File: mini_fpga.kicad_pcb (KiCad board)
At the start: 4 copper layers, 50.8 x 50.8 mm, 130 parts, among them J1 PWR_HEADER1X6, J2 1X6_HEADER, J3 1X6_HEADER, J4 JTAG_1X6, J5 USD_SLOT, J6 HDMI, U1 AP7331, U2 PAM2306D, U3 XC6SLX9, U4 IS43R86400D-6TL, U5 S25FL164, U6 CPPC7, U7 FXMHD103

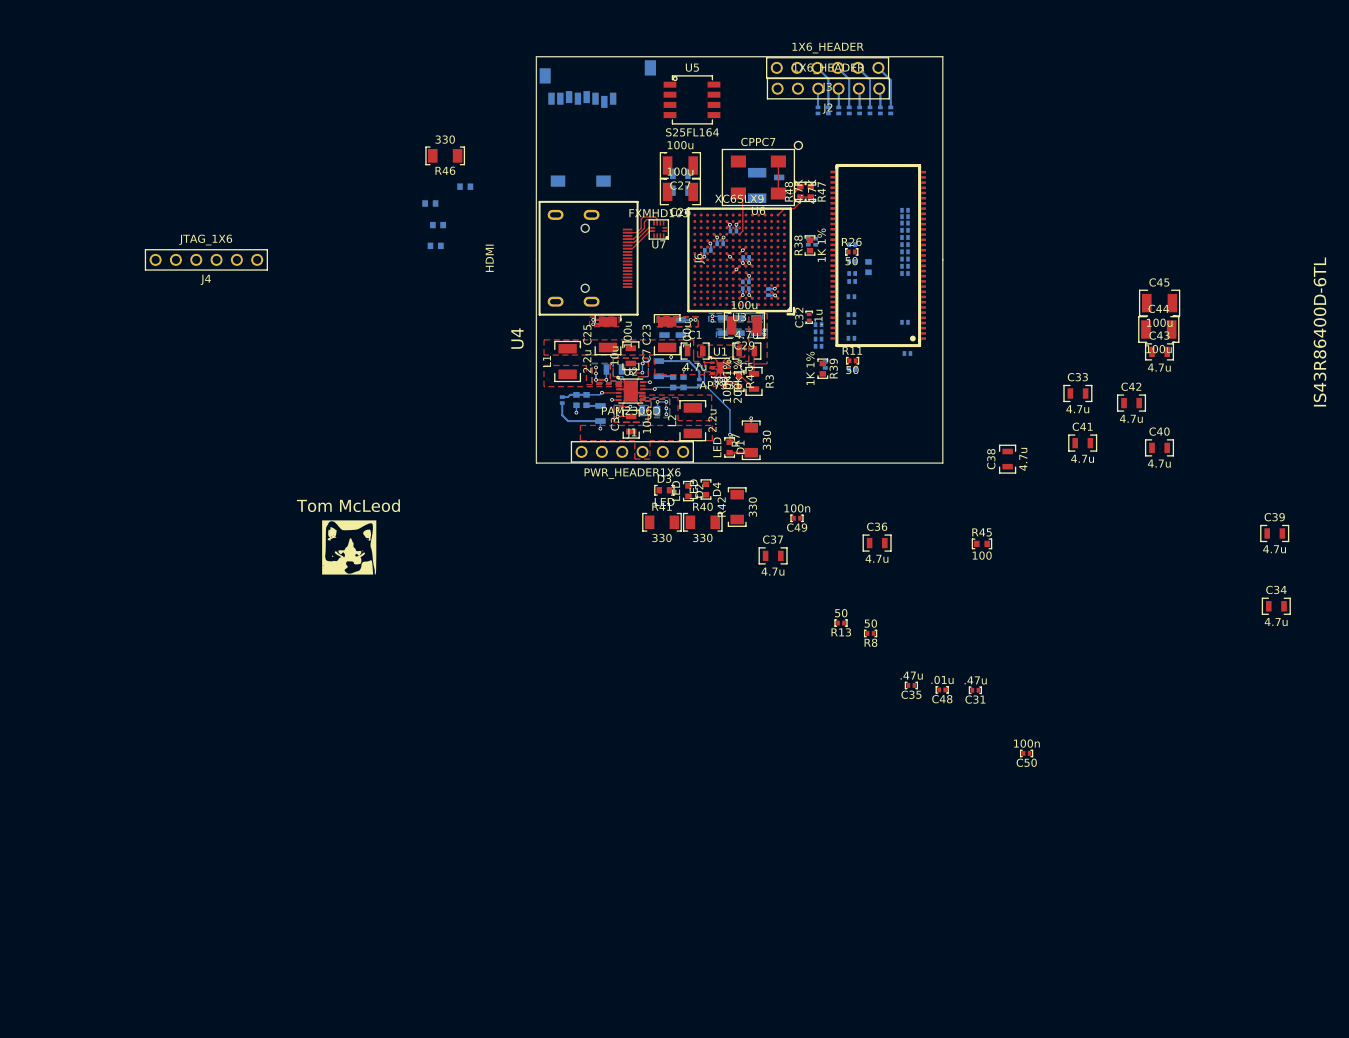
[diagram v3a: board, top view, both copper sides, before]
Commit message: Started routing DDR again using proper trace widths.
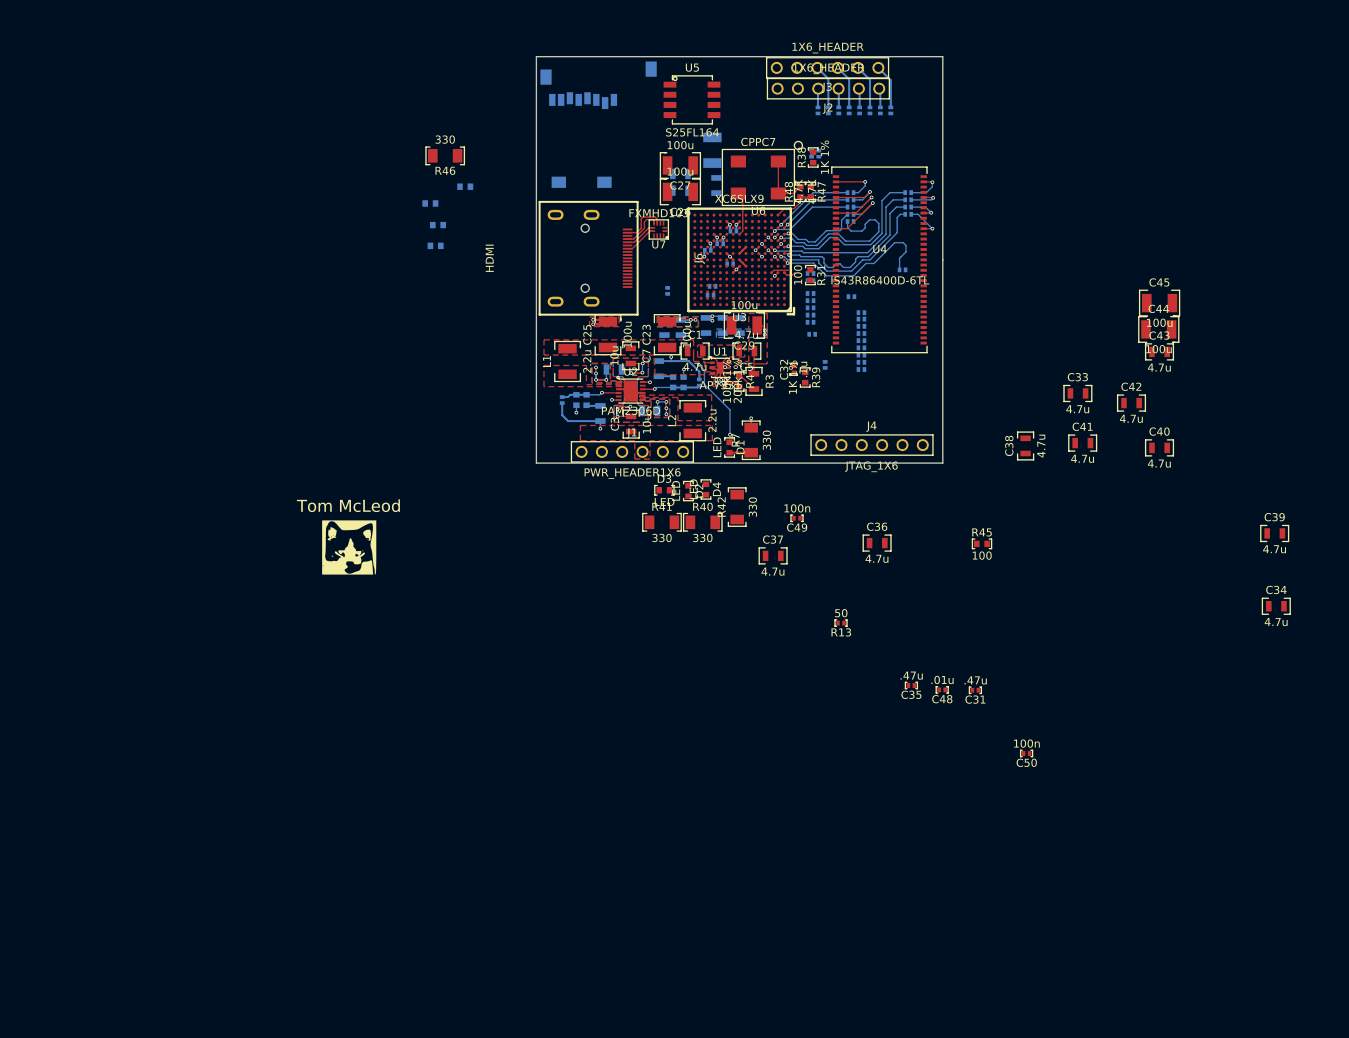
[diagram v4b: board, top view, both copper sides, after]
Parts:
- R11, R26, R8: moved to B.Cu
- R31: moved to F.Cu
- U4: footprint TSOP66 -> TSOP-66
- moved J4 86.4 mm to (194.3, 150.2), turned to 0 degrees
- moved R8 53.4 mm to (191.7, 120.4)
- moved R11 22.1 mm to (198.9, 118.6), turned to 0 degrees
- moved R15 22.1 mm to (191.7, 118.6)
- moved R16 20.5 mm to (191.7, 119.5)
- moved R19 17.9 mm to (198.9, 120.4)
- moved R10 16.0 mm to (198.9, 119.5), turned to 0 degrees
- moved R18 15.3 mm to (198.9, 121.3)
- moved R9 15.1 mm to (191.7, 121.3)
- moved R22 14.2 mm to (186.7, 128.7)
- moved R21 13.2 mm to (193.1, 139.8)
- moved R27 13.2 mm to (193.1, 135.3)
- moved R20 13.2 mm to (193.1, 138.9)
- moved R28 13.2 mm to (193.1, 134.4)
- moved R30 13.2 mm to (193.1, 133.6)
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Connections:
- net N-0000019 renamed /memory/RAM_CKE_FPGA
- net N-0000020 renamed /memory/RAM_A11_FPGA
- net N-0000021 renamed /memory/RAM_A12_FPGA
- net N-0000023 renamed /memory/RAM_DQS_FPGA
- net N-0000024 renamed /memory/RAM_DQ6_FPGA
- net N-0000027 renamed /memory/RAM_DQ0_FPGA
- net N-0000028 renamed /memory/RAM_A2_FPGA
- net N-0000029 renamed /memory/RAM_DM_FPGA
- net N-0000030 renamed /memory/RAM_A0_FPGA
- net N-0000031 renamed /memory/RAM_A1_FPGA
- net N-0000032 renamed /memory/RAM_BA0_FPGA
- net N-0000033 renamed /memory/RAM_BA1_FPGA
- net N-0000034 renamed /memory/RAM_A7_FPGA
- net N-0000035 renamed /memory/FPGA_A9_FPGA
- net N-0000036 renamed /memory/RAM_WE_FPGA
- net N-0000037 renamed /memory/RAM_A10_FPGA
- net N-0000038 renamed /memory/RAM_A4_FPGA
- net N-0000039 renamed /memory/RAM_A8_FPGA
- net N-0000041 renamed /memory/RAM_DQ1_FPGA
- net N-0000042 renamed /memory/RAM_DQ2_FPGA
- net N-0000043 renamed /memory/RAM_DQ3_FPGA
- net N-0000045 renamed /memory/RAM_DQ7_FPGA
- net N-0000046 renamed /memory/RAM_DQ4_FPGA
- net N-0000047 renamed /memory/RAM_DQ5_FPGA
- net N-0000051 renamed /memory/RAM_RAS_FPGA
- net N-0000053 renamed /memory/RAM_A5_FPGA
- net N-0000070 renamed /memory/RAM_CLK
- net N-0000071 renamed /memory/RAM_CLKN
- net N-0000089 renamed /memory/RAM_CAS_FPGA
- net N-0000090 renamed /memory/RAM_A6_FPGA
- net N-0000091 renamed /memory/RAM_A3_FPGA
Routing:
- net /memory/RAM_DQ6_FPGA: track 0.00 -> 21.7 mm, vias 0 -> 1
- net /memory/RAM_DQS_FPGA: track 0.00 -> 21.5 mm, vias 0 -> 1
- net /memory/RAM_DQ5_FPGA: track 0.00 -> 21.4 mm, vias 0 -> 1
- net /memory/RAM_DQ7_FPGA: track 0.00 -> 21.3 mm, vias 0 -> 1
- net /memory/RAM_DM_FPGA: track 0.00 -> 21.3 mm, vias 0 -> 1
- net /memory/RAM_DQ4_FPGA: track 0.00 -> 21.1 mm, vias 0 -> 1
- net /memory/RAM_DQ2_FPGA: track 0.00 -> 10.9 mm, vias 0 -> 1
- net /memory/RAM_DQ0_FPGA: track 0.00 -> 10.5 mm, vias 0 -> 1
- net /memory/RAM_DQ3_FPGA: track 0.00 -> 10.4 mm, vias 0 -> 1
- net /memory/RAM_DQ1_FPGA: track 0.00 -> 9.35 mm, vias 0 -> 1
- net /memory/RAM_DQ3: track 0.00 -> 8.91 mm, vias 0 -> 1
- net /memory/RAM_DQ2: track 0.00 -> 8.01 mm, vias 0 -> 1
- net /memory/RAM_DQ1: track 0.00 -> 7.11 mm, vias 0 -> 1
- net /memory/RAM_DQ0: track 0.00 -> 5.96 mm, vias 0 -> 1
- net /memory/RAM_DQ7: track 0.00 -> 4.63 mm, vias 0 -> 1
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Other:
- net class Memory added: clearance 0.254, trace_width 0.127, via_dia 0.4572, via_drill 0.254

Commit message: More edits to the DDR interface
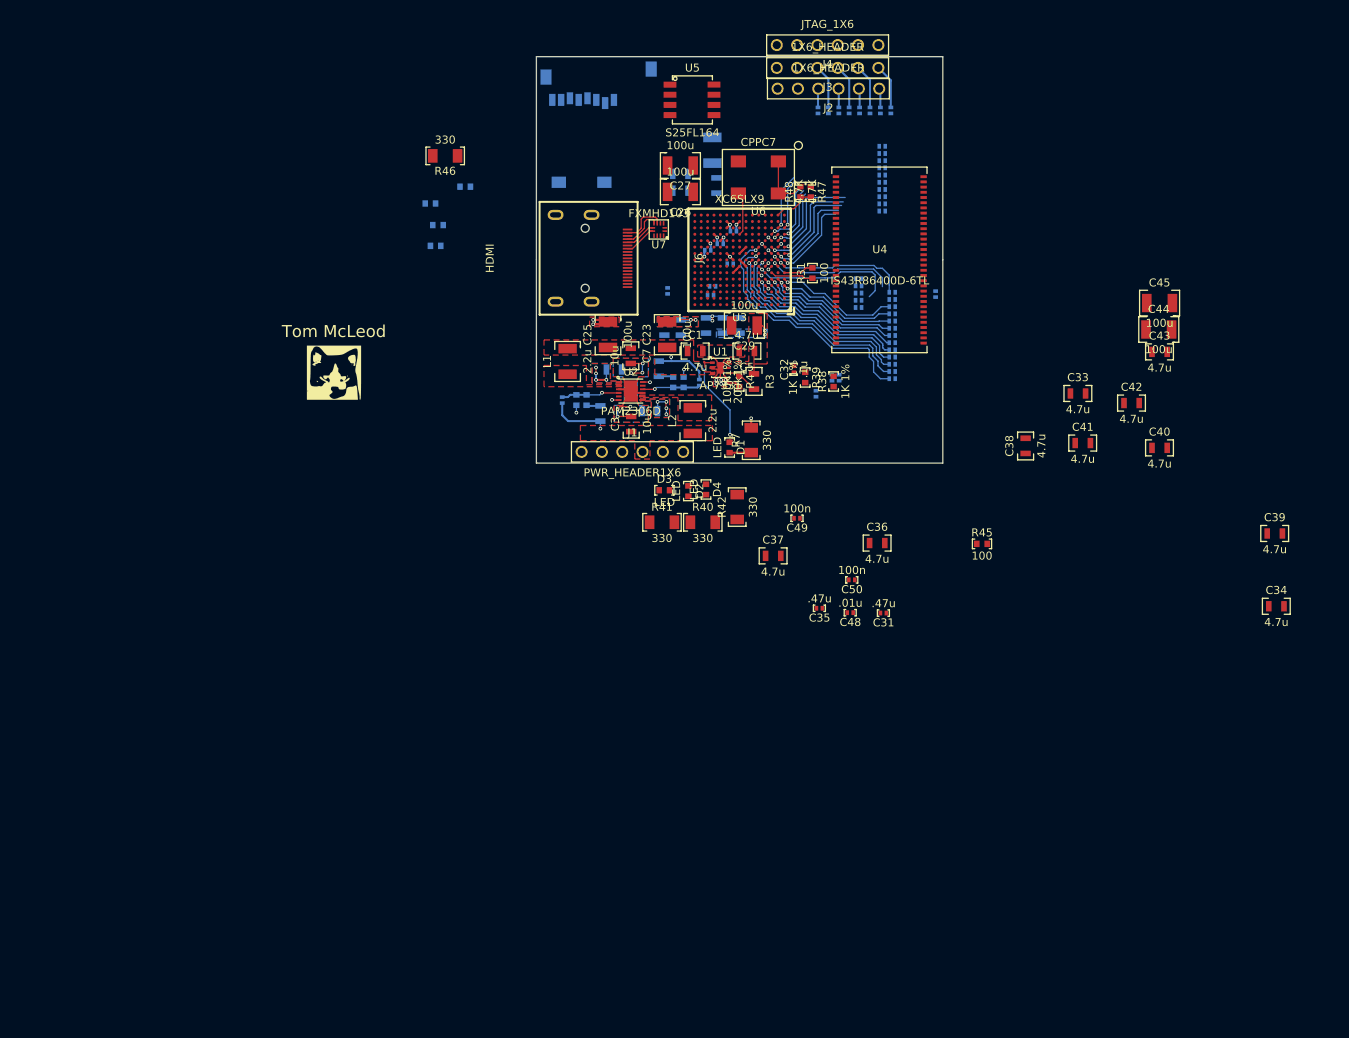
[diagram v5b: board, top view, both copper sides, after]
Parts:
- R13: moved to B.Cu
- moved J4 50.3 mm to (188.8, 100.2), turned to 180 degrees
- moved R13 41.0 mm to (196.9, 131.9)
- moved C50 30.8 mm to (191.8, 167.0)
- moved C47 28.1 mm to (190.2, 141.8)
- moved C30 28.1 mm to (189.3, 141.7)
- moved R38 28.1 mm to (189.6, 142.2)
- moved G*** 21.9 mm to (127.1, 141.1)
- moved R22 16.6 mm to (196.9, 141.8)
- moved C31 15.0 mm to (195.8, 171.2)
- moved C48 15.0 mm to (191.7, 171.1)
- moved C35 15.0 mm to (187.8, 170.6)
- moved R37 11.4 mm to (192.7, 129.3), turned to 180 degrees
- moved R29 10.7 mm to (196.9, 140.1)
- moved R25 10.5 mm to (202.3, 131.2), turned to 90 degrees
- moved R26 10.3 mm to (196.9, 135.6)
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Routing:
- net /memory/RAM_A3_FPGA: track 0.57 -> 31.3 mm
- net /memory/RAM_A0_FPGA: track 0.57 -> 29.1 mm
- net /memory/RAM_A7_FPGA: track 0.00 -> 26.1 mm, vias 0 -> 1
- net /memory/RAM_A2_FPGA: track 0.00 -> 25.3 mm, vias 0 -> 1
- net /memory/RAM_A1_FPGA: track 0.00 -> 24.0 mm, vias 0 -> 1
- net /memory/RAM_A10_FPGA: track 0.00 -> 20.1 mm, vias 0 -> 1
- net /memory/RAM_A4_FPGA: track 0.00 -> 18.7 mm, vias 0 -> 1
- net /memory/RAM_BA0_FPGA: track 0.00 -> 18.6 mm, vias 0 -> 1
- net /memory/RAM_A12_FPGA: track 0.00 -> 17.6 mm, vias 0 -> 1
- net /memory/RAM_A6_FPGA: track 0.00 -> 17.2 mm, vias 0 -> 1
- net /memory/RAM_A8_FPGA: track 0.00 -> 16.6 mm, vias 0 -> 1
- net /memory/RAM_A5_FPGA: track 0.00 -> 16.3 mm, vias 0 -> 1
- net /memory/RAM_A11_FPGA: track 0.00 -> 15.6 mm, vias 0 -> 1
- net /memory/FPGA_A9_FPGA: track 0.00 -> 15.4 mm, vias 0 -> 1
- net /memory/RAM_DQS_FPGA: track 21.5 -> 8.16 mm
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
